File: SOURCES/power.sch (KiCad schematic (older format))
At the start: 0 parts

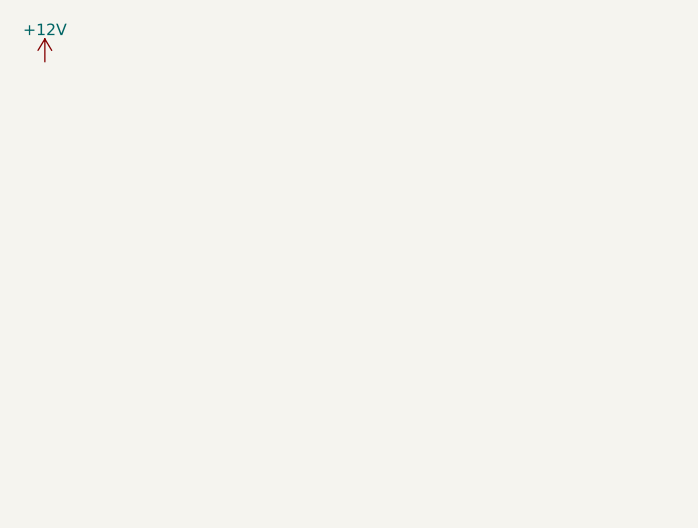
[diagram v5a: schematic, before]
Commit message: added lib power
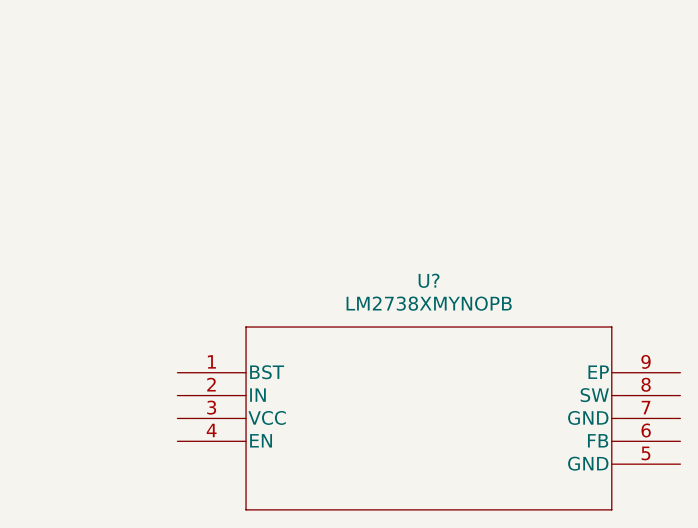
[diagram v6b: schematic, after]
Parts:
- added U?: LM2738XMYNOPB, MUY08A, symbol LM2738XMYNOPB
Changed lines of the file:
@@
 LIBS:fdsp_oscillator_new
 LIBS:fdsp_transistor_new
+LIBS:LM2738XMY&slash_NOPB-symbols
 LIBS:smd_aio-cache
 EELAYER 25 0
@@
 $EndDescr
 $Comp
-L +12V #PWR72
-U 1 1 5AFC3129
-P 4110 2290
-F 0 "#PWR72" H 4110 2140 50  0001 C CNN
-F 1 "+12V" H 4110 2430 50  0000 C CNN
-F 2 "" H 4110 2290 60  0000 C CNN
-F 3 "" H 4110 2290 60  0000 C CNN
-	1    4110 2290
+L LM2738XMYNOPB U?
+U 1 1 5B09DA97
+P 4690 3650
+F 0 "U?" H 5790 4050 60  0000 C CNN
+F 1 "LM2738XMYNOPB" H 5790 3950 60  0000 C CNN
+F 2 "MUY08A" H 5790 3890 60  0001 C CNN
+F 3 "" H 4690 3650 60  0000 C CNN
+	1    4690 3650
 	1    0    0    -1
 $EndComp

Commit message: added power
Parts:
- removed U?: LM2738XMYNOPB, MUY08A, symbol LM2738XMYNOPB
- added C? (x3): 100n, symbol C
- added C? (x4): 10u, symbol C
- added C?: 100u, symbol CP
- added C?: 150n, symbol C
- added D?: D_Schottky, symbol D_Schottky
- added D?: SMAJ28A, symbol SMAJ28A
- added D?: B150, symbol D_Schottky
- added F?: 0ZCJ0050AF2E, symbol 0ZCJ0050AF2E
- added FB?: BLM18PG471SNL, symbol FILTER
- added L?: 47u, symbol Inductor
- added P?: CONN_01X02, symbol CONN_01X02
- added R?: 1.02k, symbol R
- added R?: 3.4k, symbol R
- added U?: LM2842Y, symbol LM284x
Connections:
- new net: C?.2, U?.1 (CB)
- new net: R?.1, R?.2, U?.3 (FB)
- new net: C?.1, D?.1 (K), L?.1, U?.6 (SW)
- new net: D?.1 (K), F?.2
- new net +12V: D?.2 (A), P?.2 (P2)
- new net +3V3: C?.1, C?.1, C?.1, L?.2, R?.1
- new net GND: C?.2, C?.2, C?.2, C?.2, C?.2, C?.2, C?.2, C?.2, D?.1, D?.2 (A), P?.1 (P1), R?.2, U?.2 (GND)
- new net VCC: C?.1, C?.1, C?.1, FB?.2, U?.4 (SHDN), U?.5 (Vin)
- new net VIN: C?.1, C?.1, F?.1, FB?.1

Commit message: design rule check
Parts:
- gave numbers to parts that had none: 19
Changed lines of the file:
@@
 LIBS:fdsp_transistor_new
 LIBS:LM2738XMY&slash_NOPB-symbols
-LIBS:smd_aio-cache
 EELAYER 25 0
 EELAYER END
@@
 $EndDescr
 $Comp
-L LM284x U?
+L LM284x U7
 U 1 1 5B11E9CE
 P 6280 3220
-F 0 "U?" H 6530 3520 60  0000 C CNN
+F 0 "U7" H 6530 3520 60  0000 C CNN
 F 1 "LM2842Y" H 6180 3520 60  0000 C CNN
 F 2 "" H 6330 3220 60  0000 C CNN
@@
 $EndComp
 $Comp
-L CONN_01X02 P?
+L CONN_01X02 P13
 U 1 1 5B11EBC4
 P 790 3120
-F 0 "P?" H 790 3270 50  0000 C CNN
+F 0 "P13" H 790 3270 50  0000 C CNN
 F 1 "CONN_01X02" V 890 3120 50  0000 C CNN
 F 2 "" H 790 3120 60  0000 C CNN
@@
 $EndComp
 $Comp
-L D_Schottky D?
+L D_Schottky D6
 U 1 1 5B11EBF7
 P 1450 3070
-F 0 "D?" H 1450 3170 50  0000 C CNN
+F 0 "D6" H 1450 3170 50  0000 C CNN
 F 1 "D_Schottky" H 1450 2970 50  0000 C CNN
 F 2 "" H 1450 3070 60  0000 C CNN
@@
 $EndComp
 $Comp
-L 0ZCJ0050AF2E F?
+L 0ZCJ0050AF2E F1
 U 1 1 5B11EE09
 P 2390 2940
-F 0 "F?" H 2160 2700 60  0000 C CNN
+F 0 "F1" H 2160 2700 60  0000 C CNN
 F 1 "0ZCJ0050AF2E" H 2140 2940 60  0000 C CNN
 F 2 "" H 2140 2940 60  0001 C CNN
@@
 $EndComp
 $Comp
-L SMAJ28A D?
+L SMAJ28A D7
 U 1 1 5B11F195
 P 2940 3370
-F 0 "D?" H 2940 3370 60  0000 C CNN
+F 0 "D7" H 2940 3370 60  0000 C CNN
 F 1 "SMAJ28A" H 2940 3110 60  0000 C CNN
 F 2 "" H 2940 3370 60  0001 C CNN
@@
 $EndComp
 $Comp
-L C C?
+L C C60
 U 1 1 5B11F65D
 P 3300 3350
-F 0 "C?" H 3325 3450 50  0000 L CNN
+F 0 "C60" H 3325 3450 50  0000 L CNN
 F 1 "100n" H 3325 3250 50  0000 L CNN
 F 2 "" H 3338 3200 30  0000 C CNN
@@
 $EndComp
 $Comp
-L C C?
+L C C61
 U 1 1 5B11F680
 P 3620 3350
-F 0 "C?" H 3645 3450 50  0000 L CNN
+F 0 "C61" H 3645 3450 50  0000 L CNN
 F 1 "10u" H 3645 3250 50  0000 L CNN
 F 2 "" H 3658 3200 30  0000 C CNN
@@
 $EndComp
 $Comp
-L FILTER FB?
+L FILTER FB2
 U 1 1 5B11FC48
 P 4240 3070
-F 0 "FB?" H 4240 3220 50  0000 C CNN
+F 0 "FB2" H 4240 3220 50  0000 C CNN
 F 1 "BLM18PG471SNL" H 4240 2970 50  0000 C CNN
 F 2 "" H 4240 3070 50  0000 C CNN
@@
 $EndComp
 $Comp
-L CP C?
+L CP C62
 U 1 1 5B11FF36
 P 4900 3340
-F 0 "C?" H 4925 3440 50  0000 L CNN
+F 0 "C62" H 4925 3440 50  0000 L CNN
 F 1 "100u" H 4925 3240 50  0000 L CNN
 F 2 "" H 4938 3190 30  0000 C CNN
@@
 $EndComp
 $Comp
-L C C?
+L C C63
 U 1 1 5B120064
 P 5250 3350
-F 0 "C?" H 5275 3450 50  0000 L CNN
+F 0 "C63" H 5275 3450 50  0000 L CNN
 F 1 "10u" H 5275 3250 50  0000 L CNN
 F 2 "" H 5288 3200 30  0000 C CNN
@@
 $EndComp
 $Comp
-L C C?
+L C C64
 U 1 1 5B1200BB
 P 5520 3350
-F 0 "C?" H 5545 3450 50  0000 L CNN
+F 0 "C64" H 5545 3450 50  0000 L CNN
 F 1 "100n" H 5545 3250 50  0000 L CNN
 F 2 "" H 5558 3200 30  0000 C CNN
@@
 $EndComp
 $Comp
-L C C?
+L C C65
 U 1 1 5B122D9A
 P 7160 3070
-F 0 "C?" H 7185 3170 50  0000 L CNN
+F 0 "C65" H 7185 3170 50  0000 L CNN
 F 1 "150n" H 6940 2970 50  0000 L CNN
 F 2 "" H 7198 2920 30  0000 C CNN
@@
 $EndComp
 $Comp
-L R R?
+L R R35
 U 1 1 5B12302F
 P 7040 3610
-F 0 "R?" V 7120 3610 50  0000 C CNN
+F 0 "R35" V 7120 3610 50  0000 C CNN
 F 1 "1.02k" V 7040 3610 50  0000 C CNN
 F 2 "" V 6970 3610 30  0000 C CNN
@@
 $EndComp
 $Comp
-L D_Schottky D?
+L D_Schottky D8
 U 1 1 5B12322B
 P 7480 3610
-F 0 "D?" H 7480 3710 50  0000 C CNN
+F 0 "D8" H 7480 3710 50  0000 C CNN
 F 1 "B150" H 7480 3510 50  0000 C CNN
 F 2 "" H 7480 3610 60  0000 C CNN
@@
 $EndComp
 $Comp
-L Inductor L?
+L Inductor L5
 U 1 1 5B123304
 P 8050 3070
-F 0 "L?" H 8050 3170 50  0000 C CNN
+F 0 "L5" H 8050 3170 50  0000 C CNN
 F 1 "47u" H 8050 3020 50  0000 C CNN
 F 2 "" H 8050 3070 50  0000 C CNN
@@
 $EndComp
 $Comp
-L R R?
+L R R36
 U 1 1 5B123449
 P 8060 3370
-F 0 "R?" V 8140 3370 50  0000 C CNN
+F 0 "R36" V 8140 3370 50  0000 C CNN
 F 1 "3.4k" V 8060 3370 50  0000 C CNN
 F 2 "" V 7990 3370 30  0000 C CNN
@@
 $EndComp
 $Comp
-L C C?
+L C C66
 U 1 1 5B12369C
 P 8620 3320
-F 0 "C?" H 8645 3420 50  0000 L CNN
+F 0 "C66" H 8645 3420 50  0000 L CNN
 F 1 "100n" H 8645 3220 50  0000 L CNN
 F 2 "" H 8658 3170 30  0000 C CNN
@@
 $EndComp
 $Comp
-L C C?
+L C C67
 U 1 1 5B12374C
 P 8930 3320
-F 0 "C?" H 8955 3420 50  0000 L CNN
+F 0 "C67" H 8955 3420 50  0000 L CNN
 F 1 "10u" H 8955 3220 50  0000 L CNN
 F 2 "" H 8968 3170 30  0000 C CNN
@@
 $EndComp
 $Comp
-L C C?
+L C C68
 U 1 1 5B1237E0
 P 9270 3320
-F 0 "C?" H 9295 3420 50  0000 L CNN
+F 0 "C68" H 9295 3420 50  0000 L CNN
 F 1 "10u" H 9295 3220 50  0000 L CNN
 F 2 "" H 9308 3170 30  0000 C CNN
@@
 $EndComp
 $Comp
-L +3V3 #PWR?
+L +3V3 #PWR096
 U 1 1 5B12407E
 P 8930 3030
-F 0 "#PWR?" H 8930 2880 50  0001 C CNN
+F 0 "#PWR096" H 8930 2880 50  0001 C CNN
 F 1 "+3V3" H 8930 3170 50  0000 C CNN
 F 2 "" H 8930 3030 60  0000 C CNN
@@
 Connection ~ 8930 3830
 $Comp
-L GND #PWR?
+L GND #PWR097
 U 1 1 5B1264D3
 P 7480 3970
-F 0 "#PWR?" H 7480 3720 50  0001 C CNN
+F 0 "#PWR097" H 7480 3720 50  0001 C CNN
 F 1 "GND" H 7480 3820 50  0000 C CNN
 F 2 "" H 7480 3970 60  0000 C CNN
@@
 Connection ~ 7040 3830
 $Comp
-L VCC #PWR?
+L VCC #PWR098
 U 1 1 5B1283A5
 P 4900 3010
-F 0 "#PWR?" H 4900 2860 50  0001 C CNN
+F 0 "#PWR098" H 4900 2860 50  0001 C CNN
 F 1 "VCC" H 4900 3160 50  0000 C CNN
 F 2 "" H 4900 3010 60  0000 C CNN
@@
 $EndComp
 $Comp
-L PWR_FLAG #FLG?
+L PWR_FLAG #FLG099
 U 1 1 5B12846A
 P 5250 3020
-F 0 "#FLG?" H 5250 3115 50  0001 C CNN
+F 0 "#FLG099" H 5250 3115 50  0001 C CNN
 F 1 "PWR_FLAG" H 5250 3200 50  0000 C CNN
 F 2 "" H 5250 3020 50  0000 C CNN
@@
 $EndComp
 $Comp
-L +12V #PWR?
+L +12V #PWR0100
 U 1 1 5B12FB51
 P 1030 3040
-F 0 "#PWR?" H 1030 2890 50  0001 C CNN
+F 0 "#PWR0100" H 1030 2890 50  0001 C CNN
 F 1 "+12V" H 1030 3180 50  0000 C CNN
 F 2 "" H 1030 3040 60  0000 C CNN
@@
 $EndComp
 $Comp
-L PWR_FLAG #FLG?
+L PWR_FLAG #FLG0101
 U 1 1 5B12FD62
 P 1210 2940
-F 0 "#FLG?" H 1210 3035 50  0001 C CNN
+F 0 "#FLG0101" H 1210 3035 50  0001 C CNN
 F 1 "PWR_FLAG" H 1210 3120 50  0000 C CNN
 F 2 "" H 1210 2940 50  0000 C CNN
@@
 	1600 3070 1690 3070
 $Comp
-L VIN #PWR?
+L VIN #PWR0102
 U 1 1 5B130AA6
 P 3620 3010
-F 0 "#PWR?" H 3620 2860 50  0001 C CNN
+F 0 "#PWR0102" H 3620 2860 50  0001 C CNN
 F 1 "VIN" H 3620 3150 50  0000 C CNN
 F 2 "" H 3620 3010 60  0000 C CNN
@@
 $EndComp
 $Comp
-L PWR_FLAG #FLG?
+L PWR_FLAG #FLG0103
 U 1 1 5B130AE0
 P 3300 2990
-F 0 "#FLG?" H 3300 3085 50  0001 C CNN
+F 0 "#FLG0103" H 3300 3085 50  0001 C CNN
 F 1 "PWR_FLAG" H 3300 3170 50  0000 C CNN
 F 2 "" H 3300 2990 50  0000 C CNN
